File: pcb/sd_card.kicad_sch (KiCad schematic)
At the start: 5 parts

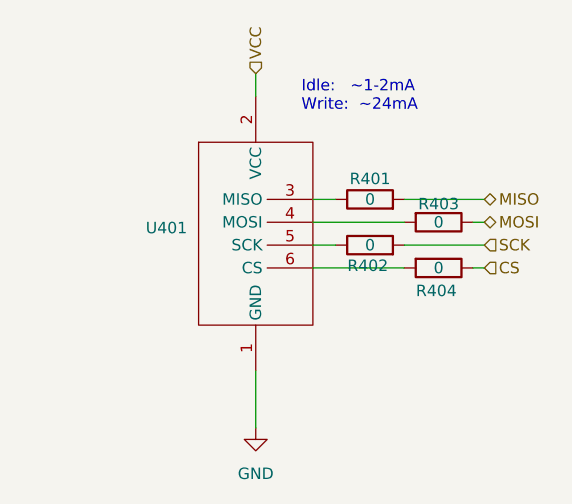
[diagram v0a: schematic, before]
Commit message: added capacitor for SD-Card
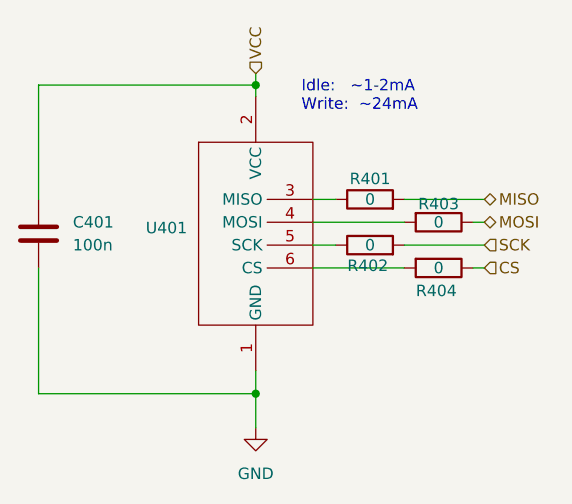
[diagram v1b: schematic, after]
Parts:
- added C401: 100n, Capacitor_SMD:C_0805_2012Metric, symbol Device:C
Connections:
- net GND: now also C401.2
- net VCC: now also C401.1
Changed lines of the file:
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@@
 		(comment 2 "Author: Leon Schnieber")
 	)
+	(junction
+		(at 130.81 104.14)
+		(diameter 0)
+		(color 0 0 0 0)
+	)
+	(junction
+		(at 130.81 69.85)
+		(diameter 0)
+		(color 0 0 0 0)
+	)
+	(wire
+		(pts
+			(xy 130.81 69.85) (xy 130.81 71.12)
+		)
+		(stroke
+			(width 0)
+			(type default)
+		)
+	)
 	(wire
 		(pts
@@
 	(wire
 		(pts
-			(xy 130.81 68.58) (xy 130.81 71.12)
+			(xy 106.68 82.55) (xy 106.68 69.85)
+		)
+		(stroke
+			(width 0)
+			(type default)
+		)
+	)
+	(wire
+		(pts
+			(xy 130.81 68.58) (xy 130.81 69.85)
 		)
 		(stroke
@@
 	(wire
 		(pts
+			(xy 130.81 104.14) (xy 130.81 107.95)
+		)
+		(stroke
+			(width 0)
+			(type default)
+		)
+	)
+	(wire
+		(pts
+			(xy 106.68 104.14) (xy 130.81 104.14)
+		)
+		(stroke
+			(width 0)
+			(type default)
+		)
+	)
+	(wire
+		(pts
 			(xy 154.94 90.17) (xy 156.21 90.17)
 		)
@@
 	(wire
 		(pts
+			(xy 106.68 90.17) (xy 106.68 104.14)
+		)
+		(stroke
+			(width 0)
+			(type default)
+		)
+	)
+	(wire
+		(pts
+			(xy 106.68 69.85) (xy 130.81 69.85)
+		)
+		(stroke
+			(width 0)
+			(type default)
+		)
+	)
+	(wire
+		(pts
 			(xy 137.16 85.09) (xy 147.32 85.09)
 		)
@@
 	(wire
 		(pts
-			(xy 130.81 101.6) (xy 130.81 107.95)
+			(xy 130.81 101.6) (xy 130.81 104.14)
 		)
 		(stroke
@@
 					(unit 1)
 				)
+			)
+		)
+	)
+	(symbol
+		(lib_id "Device:C")
+		(at 106.68 86.36 0)
+		(unit 1)
+		(exclude_from_sim no)
+		(in_bom yes)
+		(on_board yes)
+		(dnp no)
+		(fields_autoplaced yes)
+		(property "Reference" "C401"
+			(at 110.49 85.0899 0)
+			(effects
+				(font
+					(size 1.27 1.27)
+				)
+				(justify left)
+			)
+		)
+		(property "Value" "100n"
+			(at 110.49 87.6299 0)
+			(effects
+				(font
+					(size 1.27 1.27)
+				)
+				(justify left)
+			)
+		)
+		(property "Footprint" "Capacitor_SMD:C_0805_2012Metric"
+			(at 107.6452 90.17 0)
+			(effects
+				(font
+					(size 1.27 1.27)
+				)
+				(hide yes)
+			)
+		)
+		(property "Datasheet" "~"
+			(at 106.68 86.36 0)
+			(effects
+				(font
+					(size 1.27 1.27)
+				)
+				(hide yes)
+			)
+		)
+		(property "Description" "Unpolarized capacitor"
+			(at 106.68 86.36 0)
+			(effects
+				(font
+					(size 1.27 1.27)
+				)
+				(hide yes)
+			)
+		)
+		(pin "1"
+		)
+		(pin "2"
+		)
+		(instances
+			(project ""
+				(path "/278cfa6b-9496-4a22-b425-8abdb96793ef/4c18d891-44a5-41ab-9141-17f4525bee9f"
+					(reference "C401")
+					(unit 1)
+				)
